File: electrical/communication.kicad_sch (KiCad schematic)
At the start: 14 parts

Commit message: Interim check-in
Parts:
- removed PILOT_PTT_SW: SW_Push, symbol Switch:SW_Push
- added BT: DTM6R, symbol Connector:Conn_01x06_Pin
- added BT: DTM6P, symbol Connector:Conn_01x06_Socket
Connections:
- net CAN_HI_IN is gone; now on net AUDIO_IN_HI: GTR20.P2001_8 (ID_IN)
- net CAN_LO_IN is gone; now on net AUDIO_IN_LO: GTR20.P2001_6 (CAN_BUS_LO)
- net AUDIO_IN_HI: now also AUX_OUT.R, AUX_OUT.T, COPILOT_AUDIO.T, COPILOT_MIC.T, GTR20.P2001_10 (RECEIVER_AUDIO_OUT_HI), GTR20.P2001_12 (COPILOT_HS_LEFT), GTR20.P2001_14 (PILOT_HS_LEFT), GTR20.P2001_16 (COPILOT_MIC_IN), GTR20.P2001_17 (PILOT_MIC_IN), GTR20.P2001_19 (MUSIC_IN_LEFT), LEMO_COPILOT.WHT_C (COMM_L), LEMO_COPILOT.WHT_M (MIC_HI), LEMO_PILOT.WHT_C (COMM_L), LEMO_PILOT.WHT_M (MIC_HI), PILOT_AUDIO.T, PILOT_MIC.T, SW1.c1
- net AUDIO_IN_LO: now also AUX_OUT.S, COPILOT_AUDIO.R, COPILOT_MIC.S, GTR20.P2001_11 (COPILOT_HS_RIGHT), GTR20.P2001_13 (PILOT_HS_RIGHT), GTR20.P2001_18 (MUSIC_IN_RIGHT), GTR20.P2001_29 (RECEIVER_AUDIO_LO), GTR20.P2001_34 (COPILOT_MIC_LO), GTR20.P2001_36 (PILOT_MIC_LO), LEMO_COPILOT.BLU (COMM_R), LEMO_COPILOT.WH/BLU (MIC_LO), LEMO_PILOT.BLU (COMM_R), LEMO_PILOT.WH/BLU (MIC_LO), PILOT_AUDIO.R, PILOT_MIC.S, SW1.c2
- net BT_PWR: now also BT.1 (Pin_1); no longer ACX-BT.RED (12V)
- net GND: now also BT.2 (Pin_2); no longer ACX-BT.BLK (GND), LEMO_COPILOT.BLK (GND), LEMO_PILOT.BLK (GND)
- net GNDS: now reaches LEMO_PILOT.BLK/WH_C (COMM_SHIELD), LEMO_PILOT.BLK/WH_M (MIC_SHIELD), PILOT_AUDIO.G
- net GNDS: now also COPILOT_AUDIO.G, COPILOT_MIC.G, LEMO_COPILOT.BLK/WH_C (COMM_SHIELD), LEMO_COPILOT.BLK/WH_M (MIC_SHIELD), PILOT_MIC.G; no longer GTR20.P2001_33 (PILOT_HS_LO), PILOT_AUDIO.S
- net PILOT_PTT: now reaches GTR20.P2001_35 (PILOT_PTT)
- net White/Orange: now reaches GTR20.P2001_37 (MUSIC_LO), SW1.c3
- net White/Orange: now also COPILOT_AUDIO.S, GTR20.P2001_30 (COPILOT_HS_LO), GTR20.P2001_33 (PILOT_HS_LO), LEMO_COPILOT.BLK (GND), LEMO_PILOT.BLK (GND), PILOT_AUDIO.S
- net at SW1.3: now also BT.3 (Pin_3); no longer ACX-BT.GREY_T (LEFT)
- net at SW1.6: now also BT.4 (Pin_4); no longer ACX-BT.BLUE_T (RIGHT)
- net at ACX-BT.BLUE_S (RIGHT_SHIELD), ACX-BT.GREY_S (LEFT_SHIELD): now also BT.5 (Pin_5); no longer SW1.9
- new net: ACX-BT.RED (12V), BT.1 (Pin_1)
- new net: ACX-BT.BLK (GND), BT.2 (Pin_2)
- new net: ACX-BT.GREY_T (LEFT), BT.3 (Pin_3)
- new net: ACX-BT.BLUE_T (RIGHT), BT.4 (Pin_4)
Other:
- moved on the sheet: ACX-BT

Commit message: Updated from learnings from N78HR
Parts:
- removed COPILOT_MIC, PILOT_MIC: AudioJack2_Ground, symbol Connector_Audio:AudioJack2_Ground
- removed SW1: ~, symbol flyerx:SW_3P3T
- added AUDIO_SW: 4P3T, symbol flyerx:SW_4P3T_Rotary
- added COPILOT_MIC, PILOT_MIC: AudioJack3_Ground, symbol Connector_Audio:AudioJack3_Ground
- renumbered COPILOT_AUDIO to COPILOT_HS, LEMO_COPILOT to COPILOT_LEMO, PILOT_AUDIO to PILOT_HS, LEMO_PILOT to PILOT_LEMO
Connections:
- net PILOT_PTT is gone; now on net White/Orange: GTR20.P2001_35 (PILOT_PTT)
- net AUDIO_IN_HI: now also AUDIO_SW.c1, COPILOT_MIC.R, PILOT_MIC.R
- net AUDIO_IN_LO: now also COPILOT_PTT_SW.1, AUDIO_SW.c2, COPILOT_MIC.S, PILOT_MIC.S; no longer COPILOT_LEMO.WH/BLU (MIC_LO)
- net GND: no longer BT.2 (Pin_2)
- net GNDS: now also AUDIO_SW.c4, COPILOT_MIC.G, PILOT_MIC.G
- net MUSIC_IN_LEFT: now also AUDIO_SW.1
- net MUSIC_IN_LO: now also AUDIO_SW.7
- net MUSIC_IN_RIGHT: now also AUDIO_SW.4
- net White/Orange: now also COPILOT_LEMO.WH/BLU (MIC_LO), GTR20.P2001_15 (COPILOT_PTT), AUDIO_SW.c3, COPILOT_MIC.T, PILOT_MIC.T
- net at AUX_IN.R: now also AUDIO_SW.5
- net at AUX_IN.S: now also AUDIO_SW.8
- net at AUX_IN.T: now also AUDIO_SW.2
- net at BT.3 (Pin_3): now also AUDIO_SW.3
- net at BT.4 (Pin_4): now also AUDIO_SW.6
- net at BT.5 (Pin_5): now also AUDIO_SW.12
- new net: AUDIO_SW.9, BT.2 (Pin_2)
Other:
- moved on the sheet: ACX-BT, AUX_IN, AUX_OUT, BT, COMM_ANT, COPILOT_HS, COPILOT_LEMO, COPILOT_PTT_SW, GTR20, PILOT_HS, PILOT_LEMO

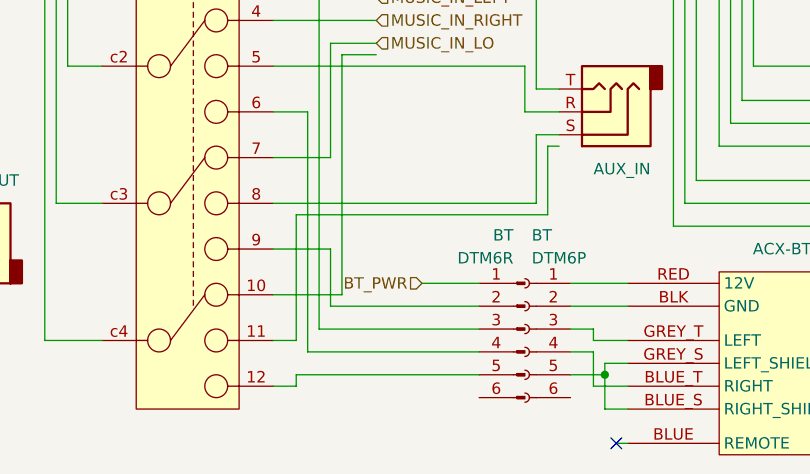
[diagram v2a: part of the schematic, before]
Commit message: Went through and changed a lot from discussions and tradeoffs. Added GTX 330, rmemoved Connext from GDU and added to GPS 175 from GDL 52. Added relay for smoke and to not use GAD 27. Added Tach sensor for SureFly. Added carb heat. Added connectors to run panel disconnected.
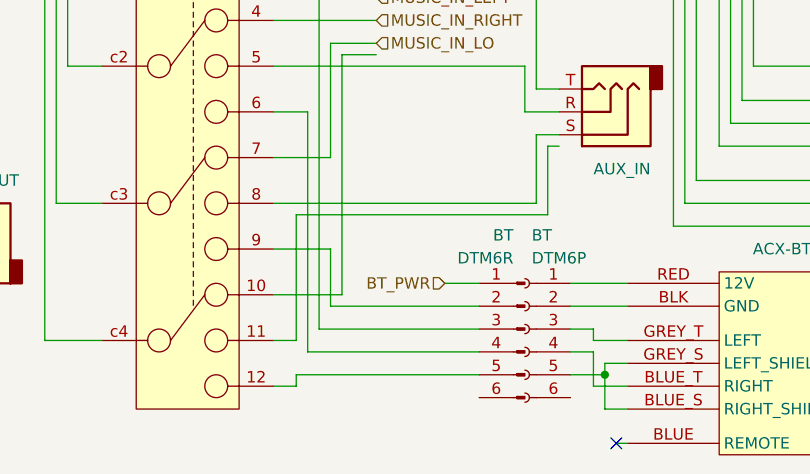
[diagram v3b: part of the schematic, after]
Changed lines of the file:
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@@
 	(wire
 		(pts
-			(xy 152.4 140.97) (xy 158.75 140.97)
+			(xy 154.94 140.97) (xy 158.75 140.97)
 		)
 		(stroke
@@
 	(hierarchical_label "BT_PWR"
 		(shape input)
-		(at 152.4 140.97 180)
-		(effects
-			(font
+		(at 154.94 140.97 180)
+		(effects
+			(font

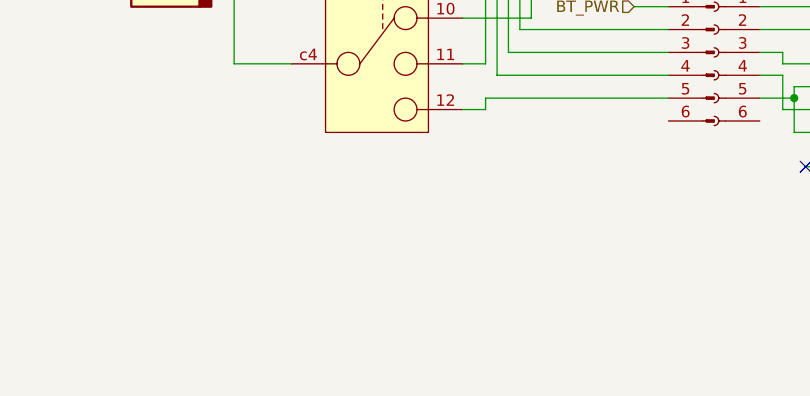
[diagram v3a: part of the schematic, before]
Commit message: Assumed engine connector is sufficient for wiring on bench..
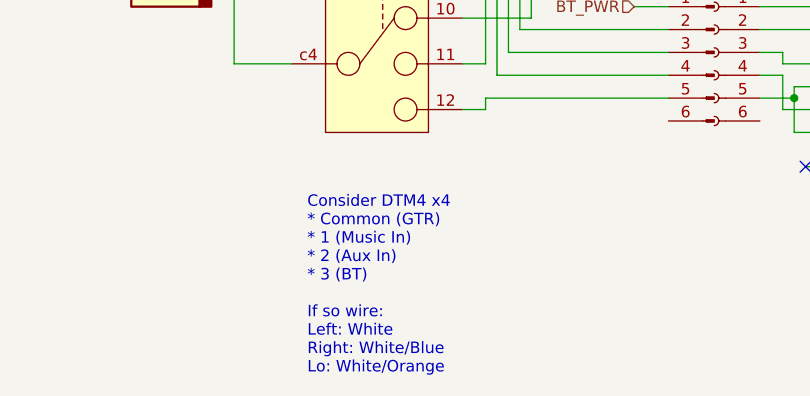
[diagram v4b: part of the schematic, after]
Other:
- note added: "Consider DTM4 x4 * Common (GTR) * 1 (Music In) * 2 (Aux In) * 3 (BT) If so wire: Left: White Right: White/Blue Lo: White/Orange"
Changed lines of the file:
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@@
 	(title_block
 		(title "Communication")
-		(date "2025-11-19")
-		(rev "1.1")
+		(date "2026-01-04")
+		(rev "1.2.4")
 		(company "N877RV")
 	)
+	(text "Consider DTM4 x4\n* Common (GTR)\n* 1 (Music In)\n* 2 (Aux In)\n* 3 (BT)\n\nIf so wire:\nLeft: White\nRight: White/Blue\nLo: White/Orange"
+		(exclude_from_sim no)
+		(at 118.618 171.958 0)
+		(effects
+			(font
+				(size 1.27 1.27)
+			)
+			(justify left)
+		)
+	)
 	(junction

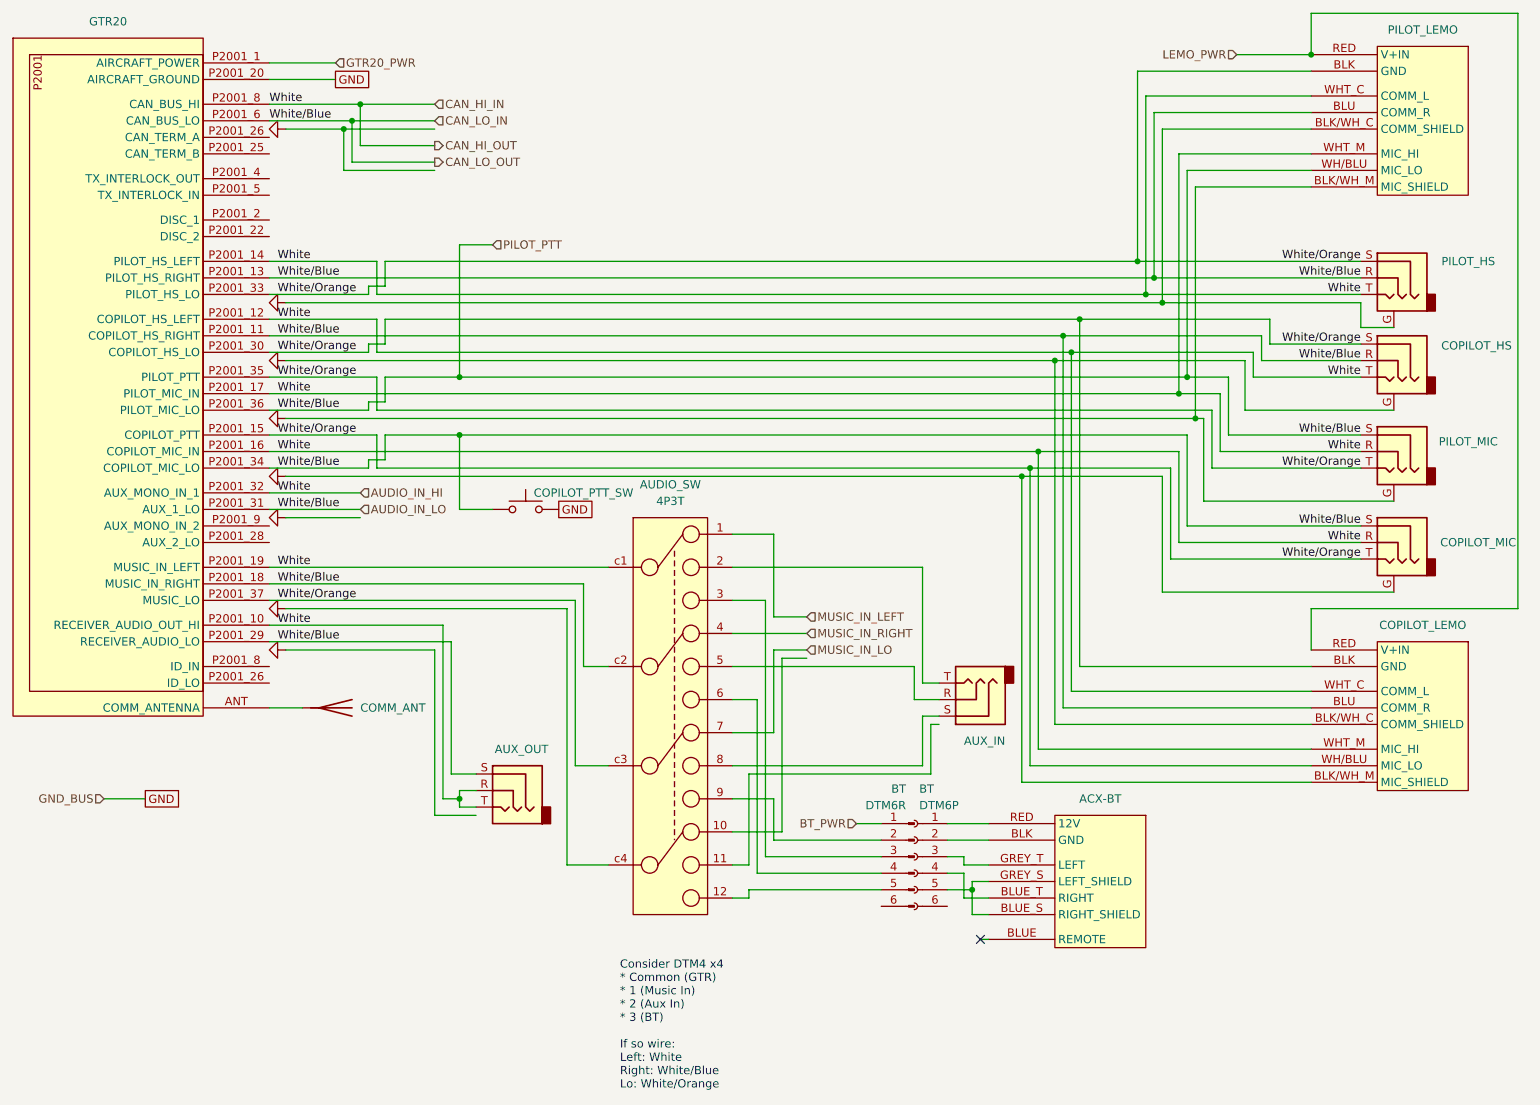
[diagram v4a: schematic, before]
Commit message: Added JST connectors as the 4P3T switch is board mount so this will be easier to connect to.
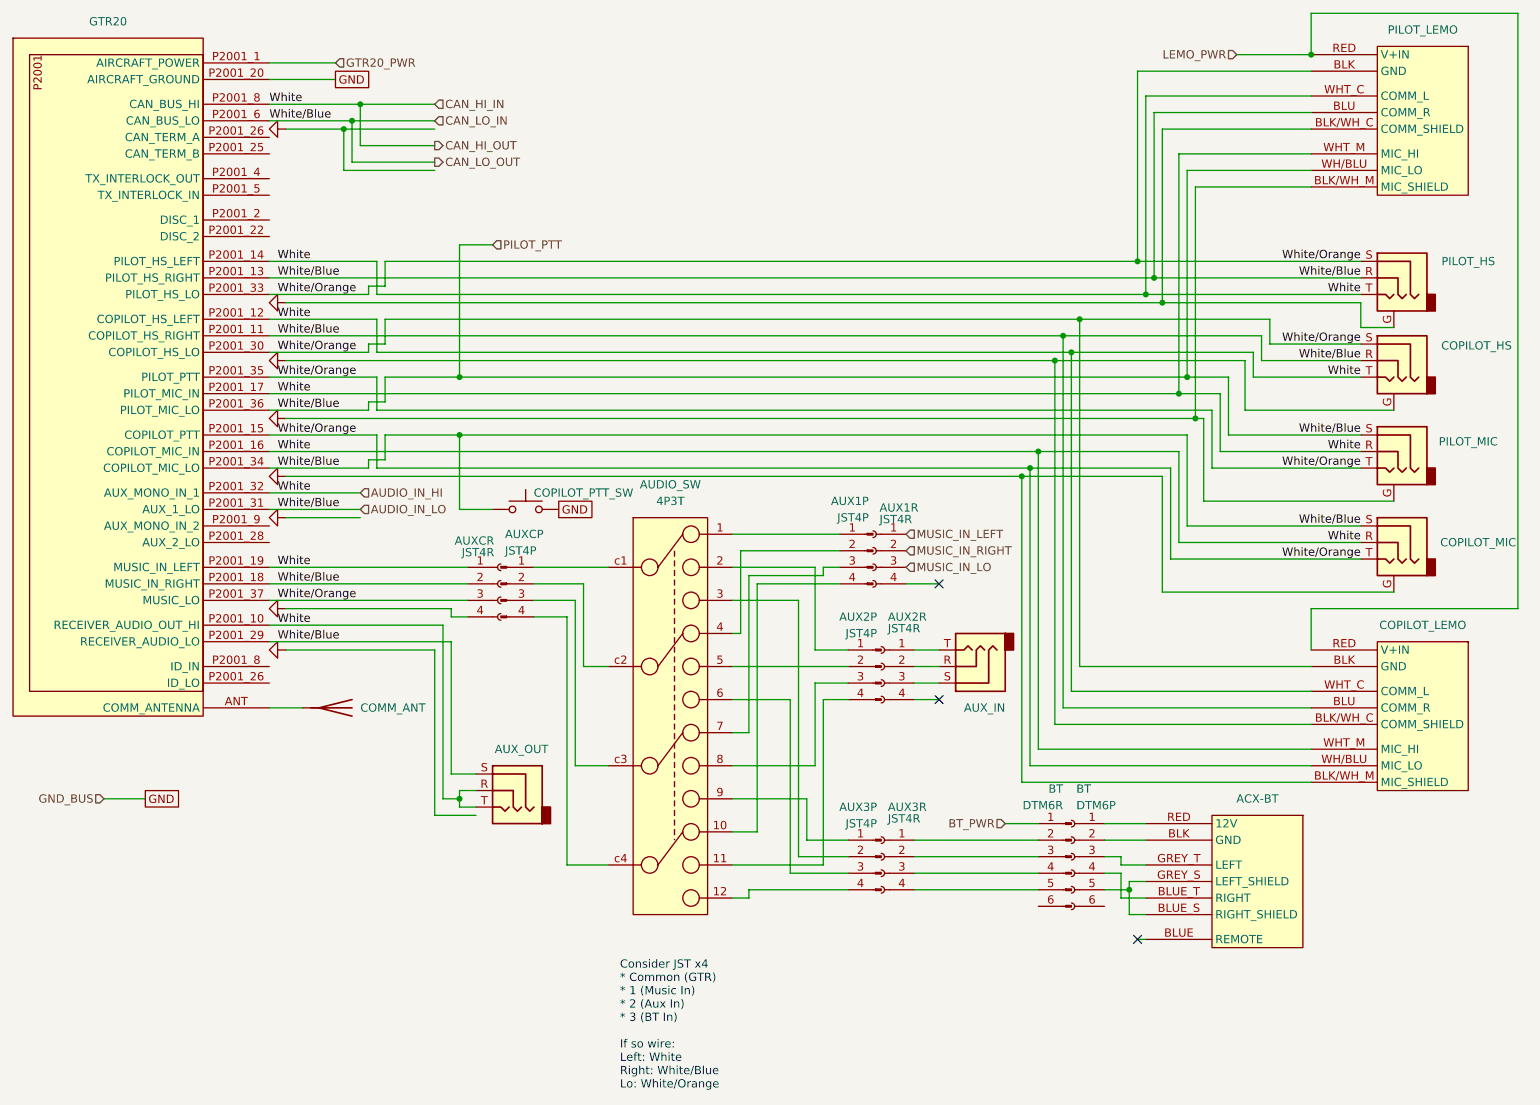
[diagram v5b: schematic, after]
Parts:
- added AUX1P, AUX2P, AUX3P, AUXCP: JST4P, symbol Connector:Conn_01x04_Pin
- added AUX1R, AUX2R, AUX3R, AUXCR: JST4R, symbol Connector:Conn_01x04_Socket
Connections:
- net AUDIO_IN_HI: now also AUXCR.1 (Pin_1); no longer AUDIO_SW.c1
- net AUDIO_IN_LO: now also AUXCR.2 (Pin_2); no longer AUDIO_SW.c2
- net GNDS: now also AUXCR.4 (Pin_4); no longer AUDIO_SW.c4
- net MUSIC_IN_LEFT: now also AUX1R.1 (Pin_1); no longer AUDIO_SW.1
- net MUSIC_IN_LO: now also AUX1R.3 (Pin_3); no longer AUDIO_SW.7
- net MUSIC_IN_RIGHT: now also AUX1R.2 (Pin_2); no longer AUDIO_SW.4
- net White/Orange: now also AUXCR.3 (Pin_3); no longer AUDIO_SW.c3
- net at AUDIO_SW.10: now also AUX1P.4 (Pin_4)
- net at AUDIO_SW.11: now also AUX2P.4 (Pin_4)
- net at AUDIO_SW.12: now also AUX3P.4 (Pin_4); no longer BT.5 (Pin_5)
- net at AUDIO_SW.2: now also AUX2P.1 (Pin_1); no longer AUX_IN.T
- net at AUDIO_SW.3: now also AUX3P.2 (Pin_2); no longer BT.3 (Pin_3)
- net at AUDIO_SW.5: now also AUX2P.2 (Pin_2); no longer AUX_IN.R
- net at AUDIO_SW.6: now also AUX3P.3 (Pin_3); no longer BT.4 (Pin_4)
- net at AUDIO_SW.8: now also AUX2P.3 (Pin_3); no longer AUX_IN.S
- net at AUDIO_SW.9: now also AUX3P.1 (Pin_1); no longer BT.2 (Pin_2)
- new net: AUDIO_SW.1, AUX1P.1 (Pin_1)
- new net: AUDIO_SW.4, AUX1P.2 (Pin_2)
- new net: AUDIO_SW.7, AUX1P.3 (Pin_3)
- new net: AUDIO_SW.c1, AUXCP.1 (Pin_1)
- new net: AUDIO_SW.c2, AUXCP.2 (Pin_2)
- new net: AUDIO_SW.c3, AUXCP.3 (Pin_3)
- new net: AUDIO_SW.c4, AUXCP.4 (Pin_4)
- new net: AUX2R.2 (Pin_2), AUX_IN.R
- new net: AUX2R.3 (Pin_3), AUX_IN.S
- new net: AUX2R.1 (Pin_1), AUX_IN.T
- new net: AUX3R.1 (Pin_1), BT.2 (Pin_2)
- new net: AUX3R.2 (Pin_2), BT.3 (Pin_3)
- new net: AUX3R.3 (Pin_3), BT.4 (Pin_4)
- new net: AUX3R.4 (Pin_4), BT.5 (Pin_5)
- no-connect marks 1 -> 3
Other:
- note added: "Consider JST x4 * Common (GTR) * 1 (Music In) * 2 (Aux In) * 3 (BT In) If so wire: Left: White Right: White/Blue Lo: White/Orange"
- note removed: "Consider DTM4 x4 * Common (GTR) * 1 (Music In) * 2 (Aux In) * 3 (BT) If so wire: Left: White Right: White/Blue Lo: White/Orange"
- moved on the sheet: ACX-BT, AUX_IN, BT

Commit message: Adde colors
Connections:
- net AUDIO_IN_HI: now also AUDIO_SW.4, AUDIO_SW.c2, AUX1P.2 (Pin_2), AUX3R.2 (Pin_2), AUXCP.2 (Pin_2), BT.3 (Pin_3)
- net Yellow: now reaches AUDIO_SW.1, AUX1P.1 (Pin_1)
- net Yellow: now also AUDIO_SW.c1, AUX3R.1 (Pin_1), AUXCP.1 (Pin_1), BT.2 (Pin_2)
- net Black: now reaches AUDIO_SW.10, AUX1P.4 (Pin_4)
- net Black: now also AUDIO_SW.c4, AUX3R.4 (Pin_4), AUXCP.4 (Pin_4), BT.5 (Pin_5)
- net Red: now reaches AUDIO_SW.7, AUX1P.3 (Pin_3)
- net Red: now also AUDIO_SW.c3, AUX3R.3 (Pin_3), AUXCP.3 (Pin_3), BT.4 (Pin_4)
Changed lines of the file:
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@@
-	(wire
-		(pts
-			(xy 135.89 96.52) (xy 152.4 96.52)
-		)
-		(stroke
-			(width 0)
-			(type default)
-		)
-	)
 	(wire
 		(pts
@@
 	(wire
 		(pts
+			(xy 152.4 96.52) (xy 135.89 96.52)
+		)
+		(stroke
+			(width 0)
+			(type default)
+		)
+	)
+	(wire
+		(pts
 			(xy 217.17 66.04) (xy 217.17 69.85)
 		)
@@
 			(width 0)
 			(type default)
+		)
+	)
+	(label "White"
+		(at 152.4 99.06 180)
+		(effects
+			(font
+				(size 1.27 1.27)
+			)
+			(justify right bottom)
 		)
 	)
@@
 		)
 	)
+	(label "Yellow"
+		(at 163.83 143.51 0)
+		(effects
+			(font
+				(size 1.27 1.27)
+			)
+			(justify left bottom)
+		)
+	)
 	(label "White{slash}Blue"
 		(at 66.04 66.04 0)
@@
 		)
 	)
+	(label "Black"
+		(at 152.4 104.14 180)
+		(effects
+			(font
+				(size 1.27 1.27)
+			)
+			(justify right bottom)
+		)
+	)
 	(label "White{slash}Blue"
 		(at 66.04 104.14 0)
+		(effects
+			(font
+				(size 1.27 1.27)
+			)
+			(justify left bottom)
+		)
+	)
+	(label "Black"
+		(at 105.41 109.22 0)
 		(effects
 			(font
@@
 		)
 	)
+	(label "Black"
+		(at 163.83 151.13 0)
+		(effects
+			(font
+				(size 1.27 1.27)
+			)
+			(justify left bottom)
+		)
+	)
+	(label "Yellow"
+		(at 152.4 96.52 180)
+		(effects
+			(font
+				(size 1.27 1.27)
+			)
+			(justify right bottom)
+		)
+	)
 	(label "White"
 		(at 66.04 83.82 0)
@@
 		)
 	)
+	(label "Red"
+		(at 105.41 106.68 0)
+		(effects
+			(font
+				(size 1.27 1.27)
+			)
+			(justify left bottom)
+		)
+	)
+	(label "White"
+		(at 163.83 146.05 0)
+		(effects
+			(font
+				(size 1.27 1.27)
+			)
+			(justify left bottom)
+		)
+	)
 	(label "White{slash}Blue"
 		(at 232.41 95.25 180)
@@
 		)
 	)
+	(label "White"
+		(at 105.41 104.14 0)
+		(effects
+			(font
+				(size 1.27 1.27)
+			)
+			(justify left bottom)
+		)
+	)
 	(label "White{slash}Blue"
 		(at 232.41 57.15 180)
@@
 			)
 			(justify right bottom)
+		)
+	)
+	(label "Red"
+		(at 152.4 101.6 180)
+		(effects
+			(font
+				(size 1.27 1.27)
+			)
+			(justify right bottom)
+		)
+	)
+	(label "Red"
+		(at 163.83 148.59 0)
+		(effects
+			(font
+				(size 1.27 1.27)
+			)
+			(justify left bottom)
 		)
 	)
@@
 		(effects
 			(font
+				(size 1.27 1.27)
+			)
+			(justify left bottom)
+		)
+	)
+	(label "Yellow"
+		(at 105.41 101.6 0)
+		(effects
+			(font
